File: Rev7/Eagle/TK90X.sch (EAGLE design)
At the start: 223 parts, among them IC1 Z80, IC10 74LS244N, IC11 LM1886, IC12 LM1889, IC13 4116, IC14 4116, IC15 4116, IC16 4116, IC17 4116, IC18 4116, IC19 4116, IC2 ROM, IC20 4116, IC21 4416, IC22 4416, IC23 4416, IC24 4416, IC25 74LS00, IC26 74LS00, IC27 74LS32, IC28 74LS04, IC29 7805, IC3 ULA TK90, IC4 74LS74, IC5 74LS74, IC6 74LS157, IC7 74LS157, IC8 74LS157, IC9 74LS157, Q1 BC548, Q2 BC548, Q3 BF494, Q4 BC548, Q5 BD139, Q6 BD136, Q7 BC548, Q8 BC517, X1 POWER, X2 EAR, X3 MIC, X4 RCA, X5 RCA, X6 LED, X7 JOYSTICK

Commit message: Corrigido valor de R49 e outros pequenos detalhes
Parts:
- R49: value 1K -> 4K7

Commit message: Pequenas correções
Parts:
- C1: value 10V100u -> 10V1000u
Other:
- moved on the sheet: C12, C13, C14, C22, C29, C31, C32, C33

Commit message: Corrigindo footprint dos jacks RCA Corrigindo lista de peças da revisão 7
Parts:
- X4, X5: device tk90:RCA2PINA1 -> tk90:RCA2PINN1

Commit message: Adicionado fotos da placa Rev 7 montada Alterado instruções para formato Markdown Corrigido capacitor C1 na placa rev. 7 Outras pequenas melhorias e correções
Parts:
- C1: device rcl:CPOL-EUE5-5 -> rcl:CPOL-EUE5-8.5
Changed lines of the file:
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@@
 <part name="X1" library="tk90" deviceset="JACKP2_S" device="" value="POWER"/>
 <part name="IC29" library="v-reg" library_urn="urn:adsk.eagle:library:409" deviceset="78XXL" device="" package3d_urn="urn:adsk.eagle:package:30361/1" value="7805"/>
-<part name="C1" library="rcl" deviceset="CPOL-EU" device="E5-5" value="10V1000u"/>
+<part name="C1" library="rcl" deviceset="CPOL-EU" device="E5-8.5" value="10V1000u"/>
 <part name="C2" library="rcl" deviceset="CPOL-EU" device="E5-6" value="25V100u"/>
 <part name="C3" library="rcl" deviceset="C-EU" device="050-024X044" value="100n"/>

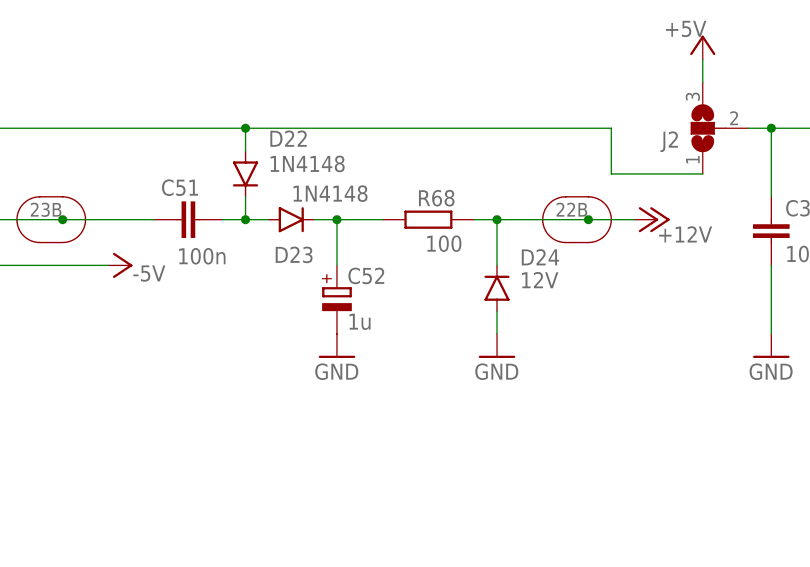
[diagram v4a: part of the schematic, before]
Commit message: Corrigido valores de R68 e C52 para melhor geração dos 12V para o Vídeo e DRAMs. Corrigido largura de algumas trilhas
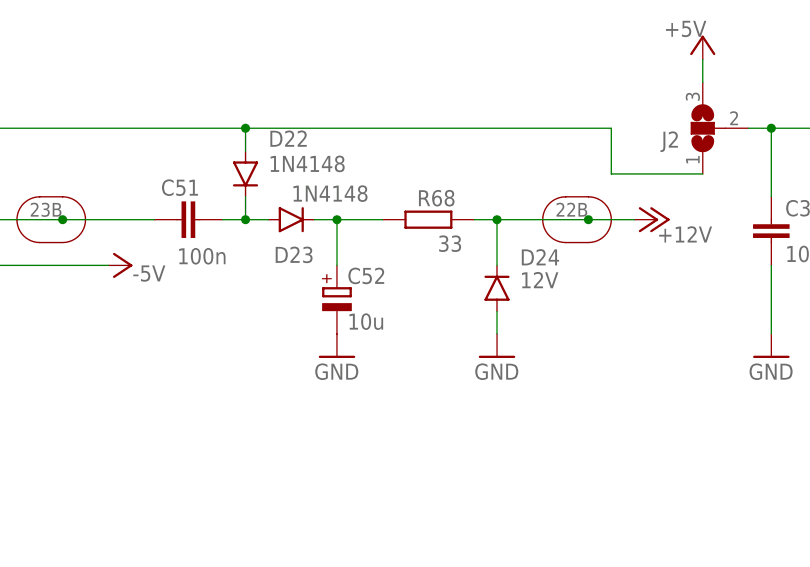
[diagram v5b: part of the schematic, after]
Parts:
- C52: value 1u -> 10u
- R68: value 100 -> 33
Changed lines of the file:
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@@
 <grid distance="0.1" unitdist="inch" unit="inch" style="lines" multiple="1" display="no" altdistance="0.01" altunitdist="inch" altunit="inch"/>
 <layers>
-<layer number="1" name="Top" color="4" fill="1" visible="yes" active="no"/>
-<layer number="2" name="Route2" color="1" fill="3" visible="yes" active="no"/>
-<layer number="3" name="Route3" color="4" fill="3" visible="yes" active="no"/>
-<layer number="4" name="Route4" color="1" fill="4" visible="yes" active="no"/>
-<layer number="5" name="Route5" color="4" fill="4" visible="yes" active="no"/>
-<layer number="6" name="Route6" color="1" fill="8" visible="yes" active="no"/>
-<layer number="7" name="Route7" color="4" fill="8" visible="yes" active="no"/>
-<layer number="8" name="Route8" color="1" fill="2" visible="yes" active="no"/>
-<layer number="9" name="Route9" color="4" fill="2" visible="yes" active="no"/>
-<layer number="10" name="Route10" color="1" fill="7" visible="yes" active="no"/>
-<layer number="11" name="Route11" color="4" fill="7" visible="yes" active="no"/>
-<layer number="12" name="Route12" color="1" fill="5" visible="yes" active="no"/>
-<layer number="13" name="Route13" color="4" fill="5" visible="yes" active="no"/>
-<layer number="14" name="Route14" color="1" fill="6" visible="yes" active="no"/>
-<layer number="15" name="Route15" color="4" fill="6" visible="yes" active="no"/>
-<layer number="16" name="Bottom" color="1" fill="1" visible="yes" active="no"/>
-<layer number="17" name="Pads" color="2" fill="1" visible="yes" active="no"/>
-<layer number="18" name="Vias" color="2" fill="1" visible="yes" active="no"/>
-<layer number="19" name="Unrouted" color="6" fill="1" visible="yes" active="no"/>
-<layer number="20" name="Dimension" color="15" fill="1" visible="yes" active="no"/>
-<layer number="21" name="tPlace" color="7" fill="1" visible="yes" active="no"/>
-<layer number="22" name="bPlace" color="7" fill="1" visible="yes" active="no"/>
-<layer number="23" name="tOrigins" color="15" fill="1" visible="yes" active="no"/>
-<layer number="24" name="bOrigins" color="15" fill="1" visible="yes" active="no"/>
-<layer number="25" name="tNames" color="7" fill="1" visible="yes" active="no"/>
-<layer number="26" name="bNames" color="7" fill="1" visible="yes" active="no"/>
-<layer number="27" name="tValues" color="9" fill="1" visible="yes" active="no"/>
-<layer number="28" name="bValues" color="7" fill="1" visible="yes" active="no"/>
+<layer number="1" name="Top" color="4" fill="1" visible="no" active="no"/>
+<layer number="2" name="Route2" color="1" fill="3" visible="no" active="no"/>
+<layer number="3" name="Route3" color="4" fill="3" visible="no" active="no"/>
+<layer number="4" name="Route4" color="1" fill="4" visible="no" active="no"/>
+<layer number="5" name="Route5" color="4" fill="4" visible="no" active="no"/>
+<layer number="6" name="Route6" color="1" fill="8" visible="no" active="no"/>
+<layer number="7" name="Route7" color="4" fill="8" visible="no" active="no"/>
+<layer number="8" name="Route8" color="1" fill="2" visible="no" active="no"/>
+<layer number="9" name="Route9" color="4" fill="2" visible="no" active="no"/>
+<layer number="10" name="Route10" color="1" fill="7" visible="no" active="no"/>
+<layer number="11" name="Route11" color="4" fill="7" visible="no" active="no"/>
+<layer number="12" name="Route12" color="1" fill="5" visible="no" active="no"/>
+<layer number="13" name="Route13" color="4" fill="5" visible="no" active="no"/>
+<layer number="14" name="Route14" color="1" fill="6" visible="no" active="no"/>
+<layer number="15" name="Route15" color="4" fill="6" visible="no" active="no"/>
+<layer number="16" name="Bottom" color="1" fill="1" visible="no" active="no"/>
+<layer number="17" name="Pads" color="2" fill="1" visible="no" active="no"/>
+<layer number="18" name="Vias" color="2" fill="1" visible="no" active="no"/>
+<layer number="19" name="Unrouted" color="6" fill="1" visible="no" active="no"/>
+<layer number="20" name="Dimension" color="15" fill="1" visible="no" active="no"/>
+<layer number="21" name="tPlace" color="7" fill="1" visible="no" active="no"/>
+<layer number="22" name="bPlace" color="7" fill="1" visible="no" active="no"/>
+<layer number="23" name="tOrigins" color="15" fill="1" visible="no" active="no"/>
+<layer number="24" name="bOrigins" color="15" fill="1" visible="no" active="no"/>
+<layer number="25" name="tNames" color="7" fill="1" visible="no" active="no"/>
+<layer number="26" name="bNames" color="7" fill="1" visible="no" active="no"/>
+<layer number="27" name="tValues" color="9" fill="1" visible="no" active="no"/>
+<layer number="28" name="bValues" color="7" fill="1" visible="no" active="no"/>
 <layer number="29" name="tStop" color="7" fill="3" visible="no" active="no"/>
 <layer number="30" name="bStop" color="7" fill="6" visible="no" active="no"/>
@@
 <layer number="35" name="tGlue" color="7" fill="4" visible="no" active="no"/>
 <layer number="36" name="bGlue" color="7" fill="5" visible="no" active="no"/>
-<layer number="37" name="tTest" color="7" fill="1" visible="yes" active="no"/>
-<layer number="38" name="bTest" color="7" fill="1" visible="yes" active="no"/>
+<layer number="37" name="tTest" color="7" fill="1" visible="no" active="no"/>
+<layer number="38" name="bTest" color="7" fill="1" visible="no" active="no"/>
 <layer number="39" name="tKeepout" color="4" fill="11" visible="no" active="no"/>
 <layer number="40" name="bKeepout" color="1" fill="11" visible="no" active="no"/>
@@
 <layer number="44" name="Drills" color="7" fill="1" visible="no" active="no"/>
 <layer number="45" name="Holes" color="7" fill="1" visible="no" active="no"/>
-<layer number="46" name="Milling" color="3" fill="1" visible="yes" active="no"/>
-<layer number="47" name="Measures" color="7" fill="1" visible="yes" active="no"/>
-<layer number="48" name="Document" color="7" fill="1" visible="yes" active="no"/>
-<layer number="49" name="Reference" color="7" fill="1" visible="yes" active="no"/>
-<layer number="50" name="dxf" color="7" fill="1" visible="yes" active="no"/>
-<layer number="51" name="tDocu" color="7" fill="1" visible="yes" active="no"/>
-<layer number="52" name="bDocu" color="7" fill="1" visible="yes" active="no"/>
-<layer number="53" name="tGND_GNDA" color="7" fill="9" visible="yes" active="no"/>
-<layer number="54" name="bGND_GNDA" color="1" fill="9" visible="yes" active="no"/>
-<layer number="56" name="wert" color="7" fill="1" visible="yes" active="no"/>
+<layer number="46" name="Milling" color="3" fill="1" visible="no" active="no"/>
+<layer number="47" name="Measures" color="7" fill="1" visible="no" active="no"/>
+<layer number="48" name="Document" color="7" fill="1" visible="no" active="no"/>
+<layer number="49" name="Reference" color="7" fill="1" visible="no" active="no"/>
+<layer number="50" name="dxf" color="7" fill="1" visible="no" active="no"/>
+<layer number="51" name="tDocu" color="7" fill="1" visible="no" active="no"/>
+<layer number="52" name="bDocu" color="7" fill="1" visible="no" active="no"/>
+<layer number="53" name="tGND_GNDA" color="7" fill="9" visible="no" active="no"/>
+<layer number="54" name="bGND_GNDA" color="1" fill="9" visible="no" active="no"/>
+<layer number="56" name="wert" color="7" fill="1" visible="no" active="no"/>
 <layer number="90" name="Modules" color="5" fill="1" visible="yes" active="yes"/>
 <layer number="91" name="Nets" color="2" fill="1" visible="yes" active="yes"/>
@@
 <part name="GND41" library="supply1" deviceset="GND" device=""/>
 <part name="P-2" library="supply1" deviceset="-5V" device=""/>
-<part name="C52" library="rcl" deviceset="CPOL-EU" device="E2-4" value="1u"/>
+<part name="C52" library="rcl" deviceset="CPOL-EU" device="E2-4" value="10u"/>
 <part name="C51" library="rcl" deviceset="C-EU" device="050-024X044" value="100n"/>
-<part name="R68" library="rcl" deviceset="R-EU_" device="0207/12" value="100"/>
+<part name="R68" library="rcl" deviceset="R-EU_" device="0207/12" value="33"/>
 <part name="GND42" library="supply1" deviceset="GND" device=""/>
 <part name="GND43" library="supply1" deviceset="GND" device=""/>
